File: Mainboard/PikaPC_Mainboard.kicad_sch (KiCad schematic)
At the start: 83 parts, among them J1 Conn_02x05_Odd_Even, J10 Conn_01x08, J11 Conn_01x08, J12 Conn_01x08, J13 Conn_01x08, J14 Conn_01x08, J15 Conn_01x08, J16 Conn_01x08, J17 Conn_01x08, J18 Conn_01x10, J19 Conn_02x05_Odd_Even, J5 DIN41612_03x32_C_Split, J6 Mini-DIN-6, J7 Mini-DIN-6, J8 Conn_01x06, J9 Conn_01x08, SW1 SW_Push_DPDT, SW2 SW_Push, U1 PPC403GA, U10 74LS07, U11 86C325, U12 GD75232N, U13 74LVC125, U14 MCP120-315GI/TO, U15 AS6C4008-55PCN, U16 AS6C4008-55PCN, U17 ATF1504, U18 T224162B, U19 T224162B, U2 SN74LVC245A, U20 T224162B, U21 T224162B, U3 SST39VF010, U4 SN74LVC245A, U5 SN74LVC245A, U6 SN74LVC245A, U7 8042 PS/2, U8 ATF22V10C, U9 74LS04, Y1 25M, Y2 7M3728, Y3 14M31818

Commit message: ViRGE schematic/layout cleanup
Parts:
- removed R12, R13, R14, R15, R16: 10k, Resistor_THT:R_Axial_DIN0204_L3.6mm_D1.6mm_P2.54mm_Vertical, symbol Device:R_Small_US
- removed R4: 147R, Resistor_THT:R_Axial_DIN0204_L3.6mm_D1.6mm_P2.54mm_Vertical, symbol Device:R_Small_US
- added R2: 220R, Resistor_THT:R_Axial_DIN0204_L3.6mm_D1.6mm_P2.54mm_Vertical, symbol Device:R_Small_US
- added R3: 470R, Resistor_THT:R_Axial_DIN0204_L3.6mm_D1.6mm_P2.54mm_Vertical, symbol Device:R_Small_US
- added RN5: 9A103J, Resistor_THT:R_Array_SIP9, symbol Device:R_Network08_US
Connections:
- net GND: now also R2.2, R3.2, RN5.1 (common)
- net INT0: now also RN5.7 (R6); no longer RN3.3 (R2)
- net INT1: now also U7.35 (KB-OBFO), RN5.8 (R7); no longer RN3.4 (R3)
- net INT2: now also U7.36 (MS-OBFO), RN5.9 (R8); no longer RN3.5 (R4)
- net PD1: now also RN5.2 (R1)
- net PD2: now also RN5.3 (R2)
- net PD4: now also RN5.4 (R3)
- net PD5: now also RN5.5 (R4)
- net PD6: now also RN5.6 (R5)
- net RSET: now also R2.1, R3.1
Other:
- note added: "RSET Target: 147R"
- moved on the sheet: C24, RN4, U10G, U11E, U9G

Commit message: ViRGE Strapping pulldowns should be on VMD not PD
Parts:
- added RN6: 9A103J, Resistor_THT:R_Array_SIP9, symbol Device:R_Network08_US
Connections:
- net GND: now also RN6.1 (common)
- net PD1: no longer RN5.2 (R1)
- net PD2: no longer RN5.3 (R2)
- net PD4: no longer RN5.4 (R3)
- net PD5: no longer RN5.5 (R4)
- net PD6: no longer RN5.6 (R5)
- net VMD1: now also RN6.2 (R1)
- net VMD2: now also RN6.3 (R2)
- net VMD4: now also RN6.4 (R3)
- net VMD5: now also RN6.5 (R4)
- net VMD6: now also RN6.6 (R5)
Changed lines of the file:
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@@
 	(wire
 		(pts
-			(xy 863.6 182.88) (xy 876.3 182.88)
+			(xy 1193.8 276.86) (xy 1206.5 276.86)
 		)
 		(stroke
@@
 	(wire
 		(pts
-			(xy 863.6 177.8) (xy 876.3 177.8)
+			(xy 1193.8 271.78) (xy 1206.5 271.78)
 		)
 		(stroke
@@
 	(wire
 		(pts
-			(xy 863.6 180.34) (xy 876.3 180.34)
+			(xy 1193.8 274.32) (xy 1206.5 274.32)
 		)
 		(stroke
@@
 	(wire
 		(pts
-			(xy 863.6 172.72) (xy 876.3 172.72)
+			(xy 1193.8 266.7) (xy 1206.5 266.7)
 		)
 		(stroke
@@
 	(wire
 		(pts
-			(xy 863.6 175.26) (xy 876.3 175.26)
+			(xy 1193.8 269.24) (xy 1206.5 269.24)
 		)
 		(stroke
@@
 		)
 	)
-	(label "PD1"
-		(at 863.6 172.72 0)
+	(label "VMD1"
+		(at 1193.8 266.7 0)
 		(effects
 			(font
@@
 		)
 	)
-	(label "PD2"
-		(at 863.6 175.26 0)
+	(label "VMD2"
+		(at 1193.8 269.24 0)
 		(effects
 			(font
@@
 		)
 	)
-	(label "PD6"
-		(at 863.6 182.88 0)
+	(label "VMD6"
+		(at 1193.8 276.86 0)
 		(effects
 			(font
@@
 		)
 	)
-	(label "PD5"
-		(at 863.6 180.34 0)
+	(label "VMD5"
+		(at 1193.8 274.32 0)
 		(effects
 			(font
@@
 		)
 	)
-	(label "PD4"
-		(at 863.6 177.8 0)
+	(label "VMD4"
+		(at 1193.8 271.78 0)
 		(effects
 			(font
@@
 	(symbol
 		(lib_id "power:GND")
+		(at 1216.66 266.7 90)
+		(unit 1)
+		(exclude_from_sim no)
+		(in_bom yes)
+		(on_board yes)
+		(dnp no)
+		(property "Reference" "#PWR069"
+			(at 1223.01 266.7 0)
+			(effects
+				(font
+					(size 1.27 1.27)
+				)
+				(hide yes)
+			)
+		)
+		(property "Value" "GND"
+			(at 1221.74 266.7 90)
+			(effects
+				(font
+					(size 1.27 1.27)
+				)
+			)
+		)
+		(property "Footprint" ""
+			(at 1216.66 266.7 0)
+			(effects
+				(font
+					(size 1.27 1.27)
+				)
+				(hide yes)
+			)
+		)
+		(property "Datasheet" ""
+			(at 1216.66 266.7 0)
+			(effects
+				(font
+					(size 1.27 1.27)
+				)
+				(hide yes)
+			)
+		)
+		(property "Description" "Power symbol creates a global label with name \"GND\" , ground"
+			(at 1216.66 266.7 0)
+			(effects
+				(font
+					(size 1.27 1.27)
+				)
+				(hide yes)
+			)
+		)
+		(pin "1"
+		)
+		(instances
+			(project "PikaPC_Mainboard"
+				(path "/31647a00-1631-4687-a4ca-8a073377aae5"
+					(reference "#PWR069")
+					(unit 1)
+				)
+			)
+		)
+	)
+	(symbol
+		(lib_id "power:GND")
 		(at 1087.12 200.66 270)
 		(unit 1)
@@
 				)
 			)
+		)
+	)
+	(symbol
+		(lib_id "Device:R_Network08_US")
+		(at 1211.58 276.86 270)
+		(unit 1)
+		(exclude_from_sim no)
+		(in_bom yes)
+		(on_board yes)
+		(dnp no)
+		(fields_autoplaced yes)
+		(property "Reference" "RN6"
+			(at 1211.326 261.2855 90)
+			(effects
+				(font
+					(size 1.27 1.27)
+				)
+			)
+		)
+		(property "Value" "9A103J"
+			(at 1211.326 263.7098 90)
+			(effects
+				(font
+					(size 1.27 1.27)
+				)
+			)
+		)
+		(property "Footprint" "Resistor_THT:R_Array_SIP9"
+			(at 1211.58 288.925 90)
+			(effects
+				(font
+					(size 1.27 1.27)
+				)
+				(hide yes)
+			)
+		)
+		(property "Datasheet" "http://www.vishay.com/docs/31509/csc.pdf"
+			(at 1211.58 276.86 0)
+			(effects
+				(font
+					(size 1.27 1.27)
+				)
+				(hide yes)
+			)
+		)
+		(property "Description" "8 resistor network, star topology, bussed resistors, small US symbol"
+			(at 1211.58 276.86 0)
+			(effects
+				(font
+					(size 1.27 1.27)
+				)
+				(hide yes)
+			)
+		)
+		(pin "5"
+		)
+		(pin "8"
+		)
+		(pin "7"
+		)
+		(pin "3"
+		)
+		(pin "1"
+		)
+		(pin "4"
+		)
+		(pin "6"
+		)
+		(pin "2"
+		)
+		(pin "9"
+		)
+		(instances
+			(project "PikaPC_Mainboard"
+				(path "/31647a00-1631-4687-a4ca-8a073377aae5"
+					(reference "RN6")
+					(unit 1)
+				)
+			)

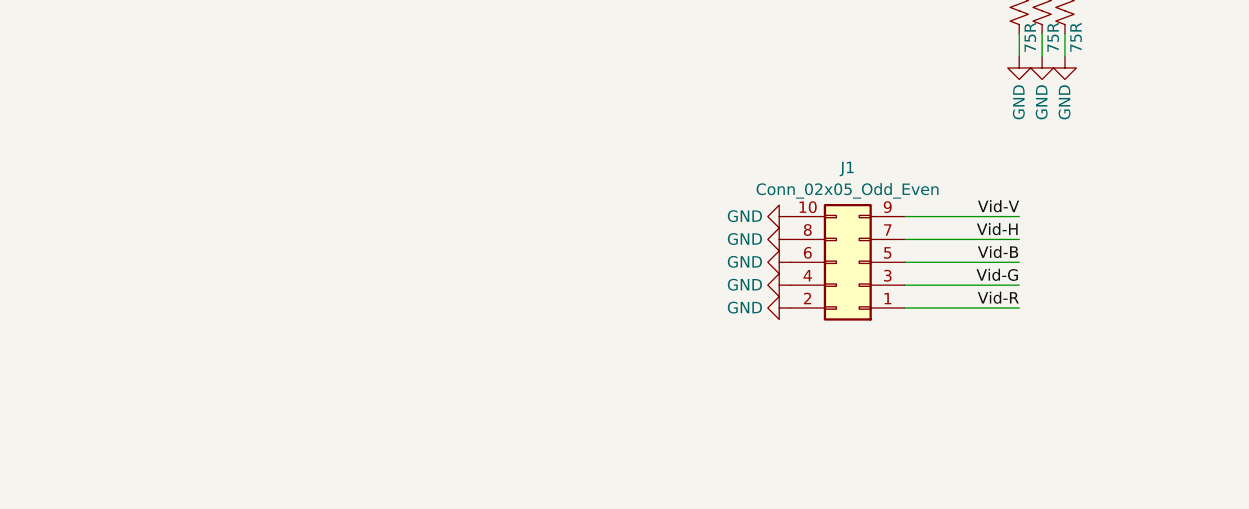
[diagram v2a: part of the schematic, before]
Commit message: VGA output use full-size header, add ferrite beads
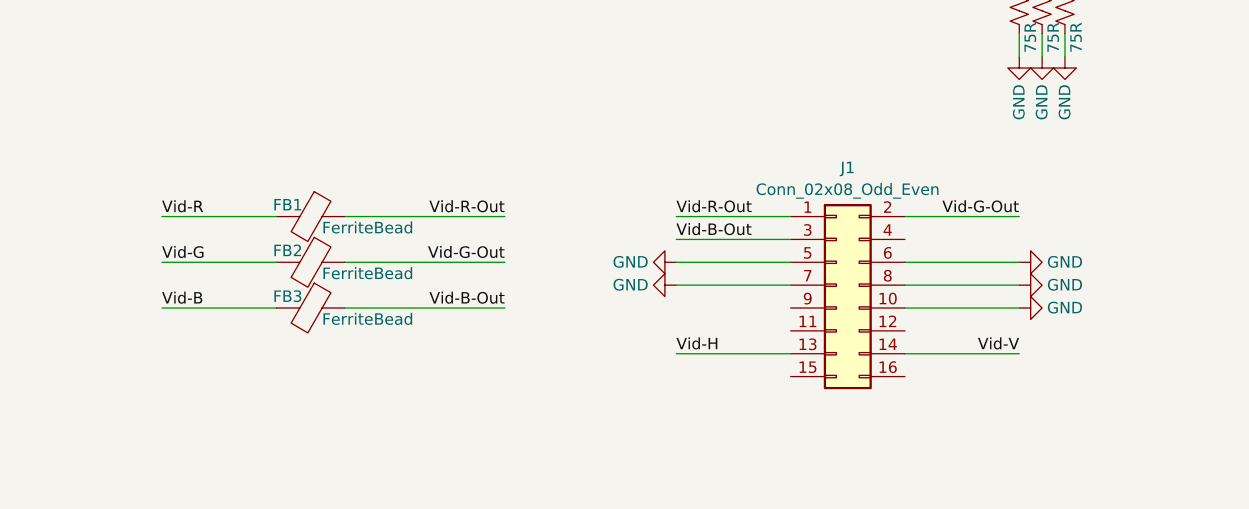
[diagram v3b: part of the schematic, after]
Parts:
- removed J1: Conn_02x05_Odd_Even, Connector_PinHeader_2.54mm:PinHeader_2x05_P2.54mm_Vertical, symbol Connector_Generic:Conn_02x05_Odd_Even
- added FB1, FB2, FB3: FerriteBead, Inductor_THT:L_Axial_L7.0mm_D3.3mm_P5.08mm_Vertical_Fastron_MICC, symbol Device:FerriteBead
- added J1: Conn_02x08_Odd_Even, Connector_PinHeader_2.54mm:PinHeader_2x08_P2.54mm_Vertical, symbol Connector_Generic:Conn_02x08_Odd_Even
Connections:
- net GND: now also J1.10 (Pin_10), J1.5 (Pin_5), J1.6 (Pin_6), J1.7 (Pin_7), J1.8 (Pin_8)
- net Vid-B: now also FB3.2
- net Vid-G: now also FB2.2
- net Vid-H: now also J1.13 (Pin_13)
- net Vid-R: now also FB1.2
- net Vid-V: now also J1.14 (Pin_14)
- new net Vid-B-Out: FB3.1, J1.3 (Pin_3)
- new net Vid-G-Out: FB2.1, J1.2 (Pin_2)
- new net Vid-R-Out: FB1.1, J1.1 (Pin_1)

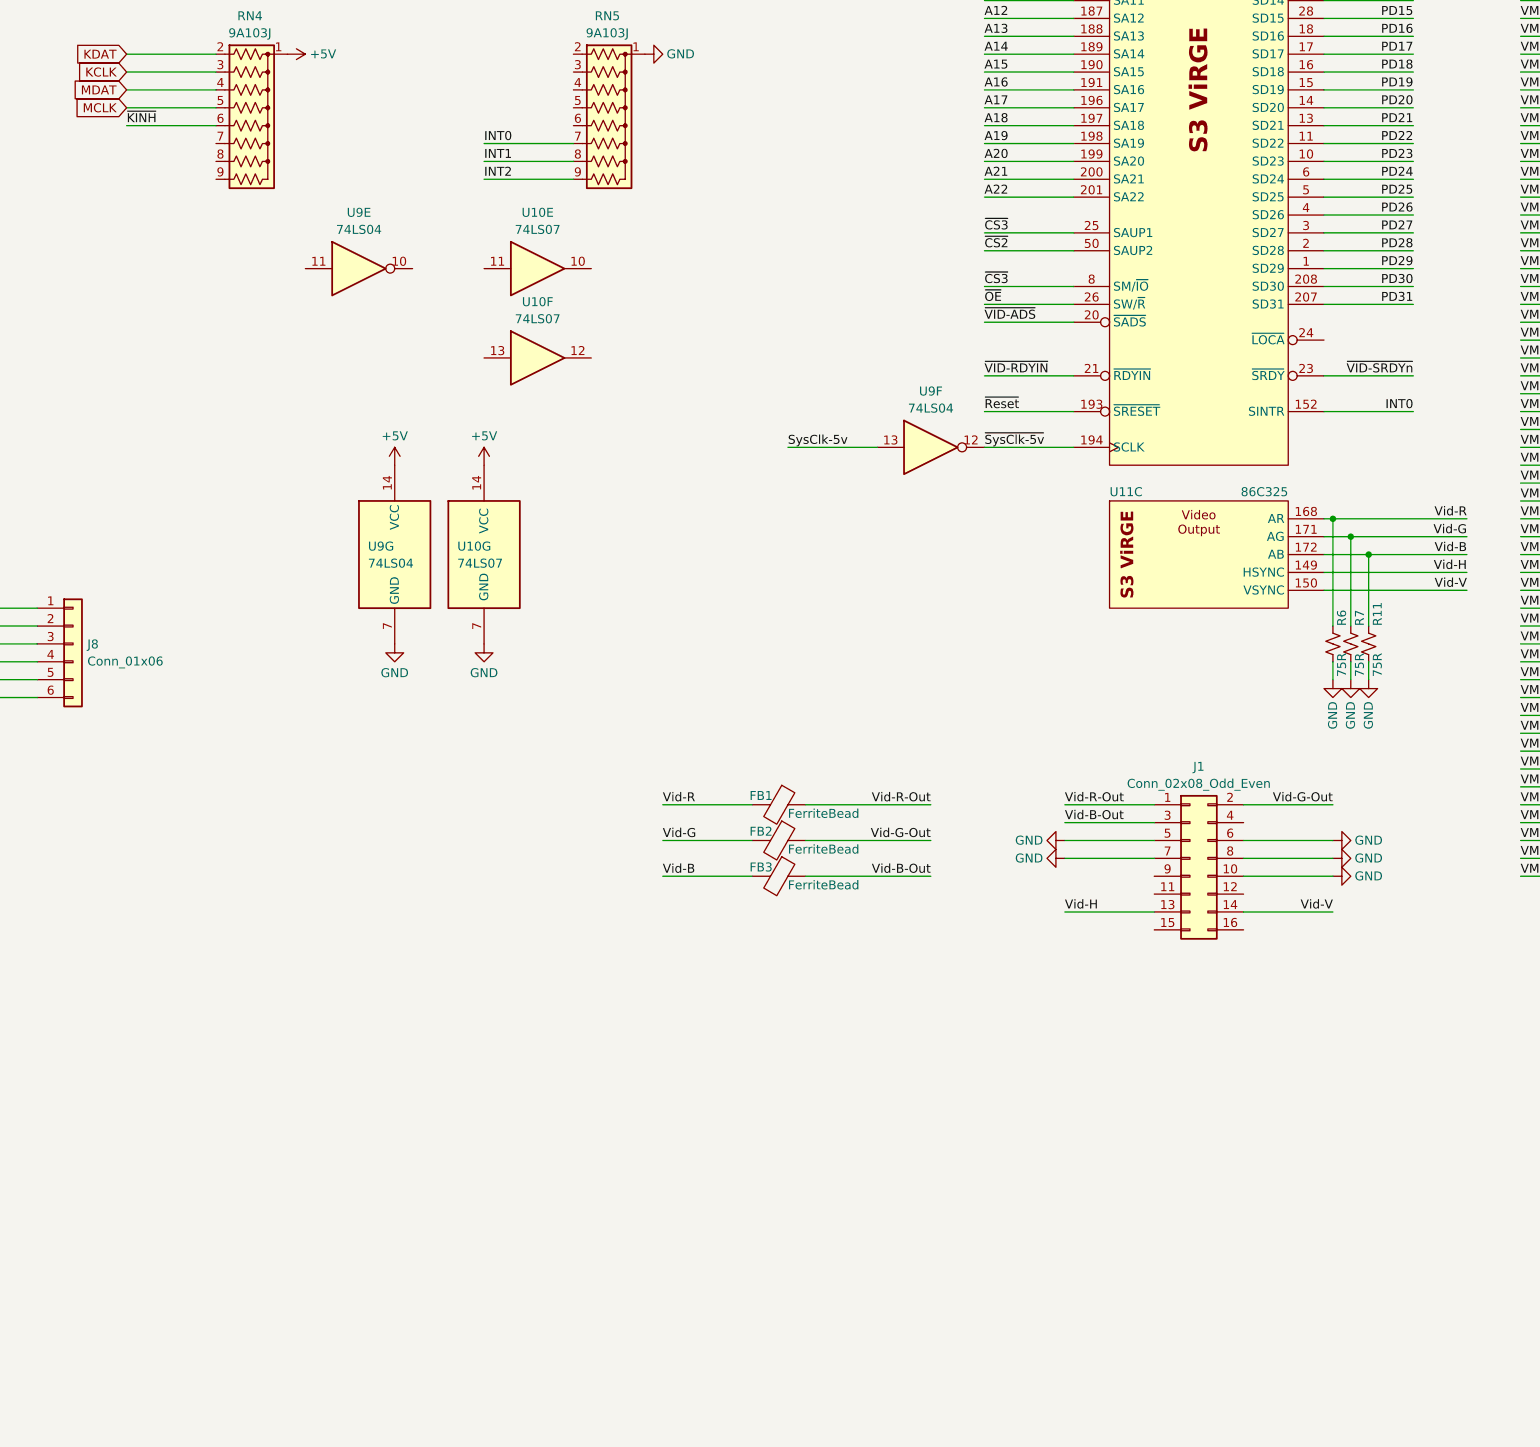
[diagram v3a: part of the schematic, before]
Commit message: Troubleshooting ViRGE communication
- use A[25:23] for ViRGE SAUP[2:1] & M/IO# signals
- add pull-up resistors to ViRGE ready & loca signals
- adjust bank registers for new memory map
- add forth test program for VGA init & ID
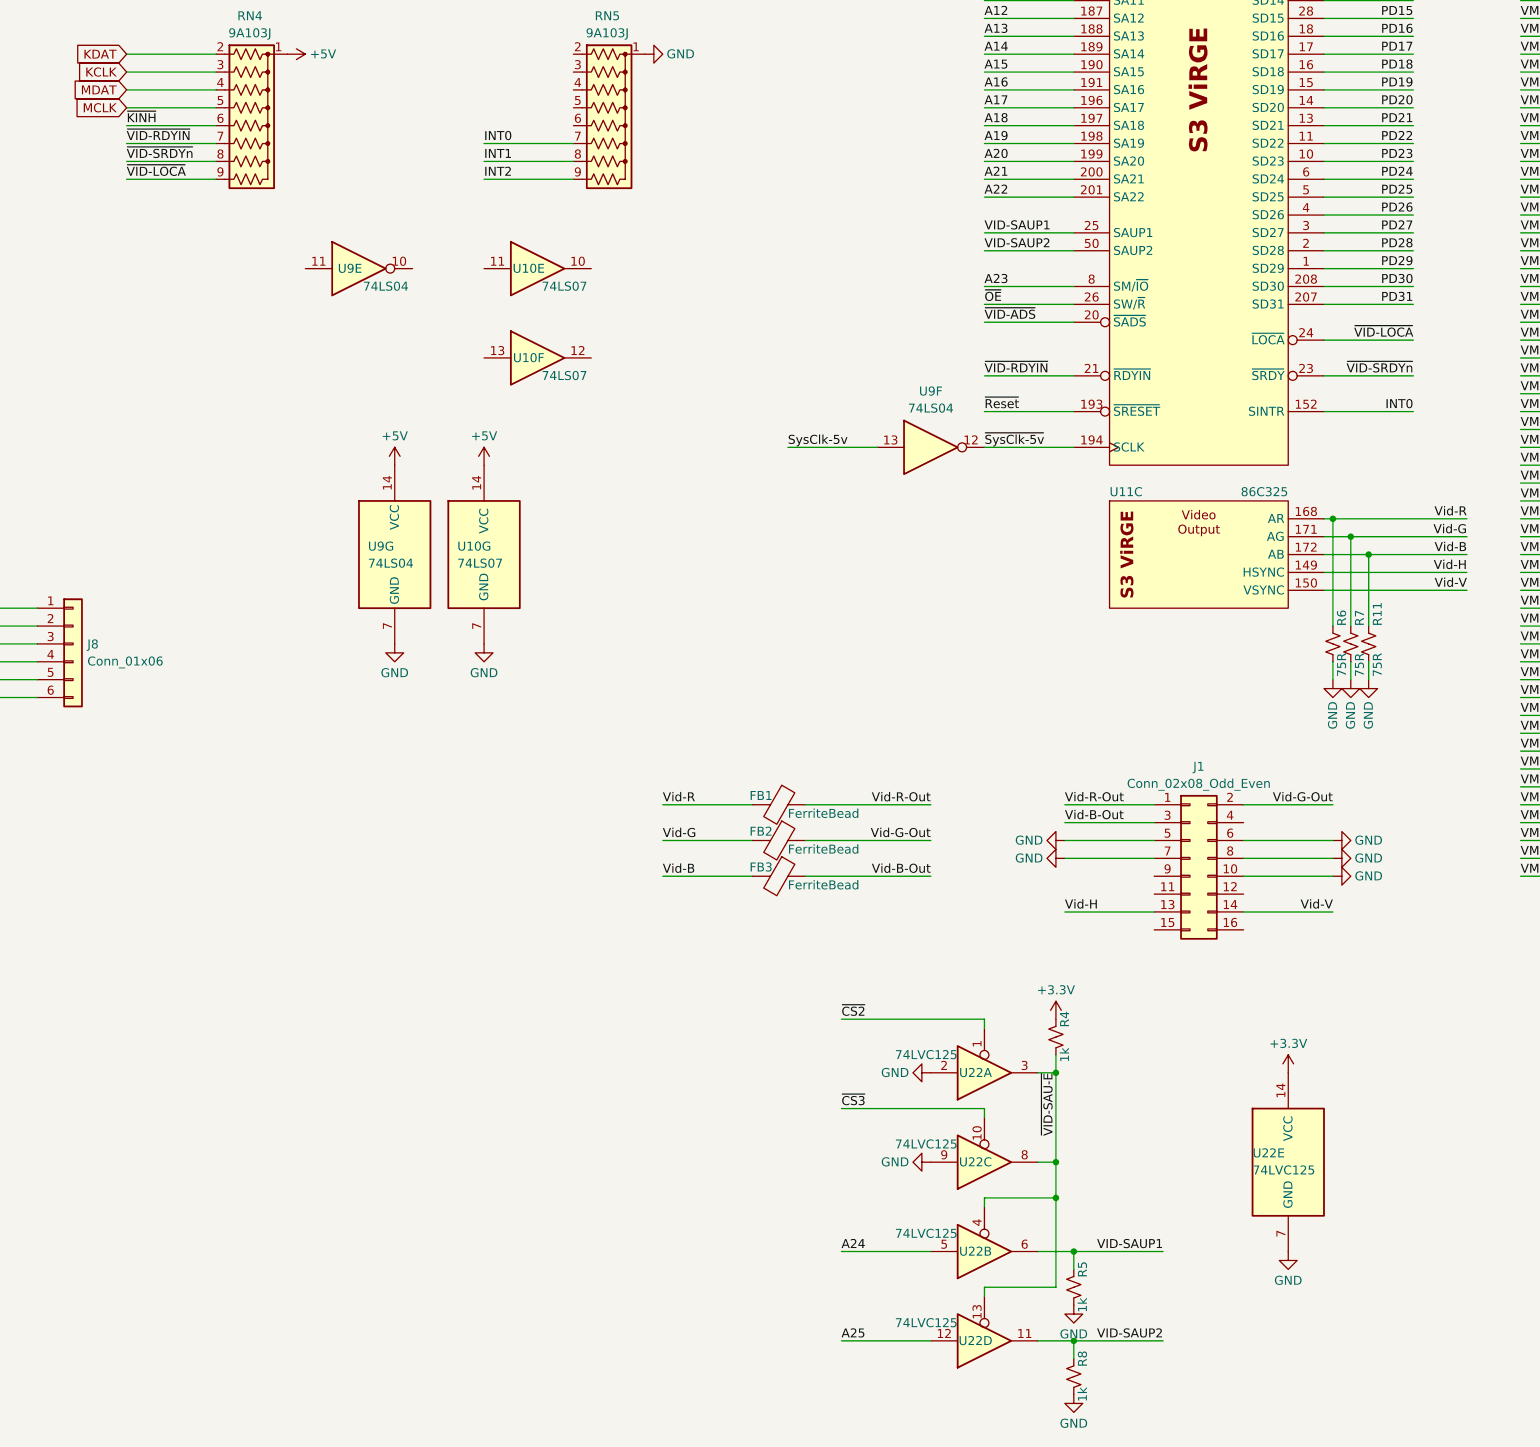
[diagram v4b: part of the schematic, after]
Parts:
- added R4, R5, R8: 1k, Resistor_THT:R_Axial_DIN0204_L3.6mm_D1.6mm_P7.62mm_Horizontal, symbol Device:R_Small_US
- added U22: 74LVC125, Package_DIP:DIP-14_W7.62mm_Socket, symbol 74xx:74LVC125
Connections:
- net +3.3V: now also R4.2, U22.14 (VCC)
- net A23: now also U11.8 (SM/~{IO})
- net A24: now also U22.5
- net A25: now also U22.12
- net GND: now also R5.1, R8.1, U22.2, U22.7 (GND), U22.9
- net ~{CS2}: now also U22.1; no longer U11.50 (SAUP2)
- net ~{CS3}: now also U22.10; no longer U11.25 (SAUP1), U11.8 (SM/~{IO})
- net ~{VID-RDYIN}: now also RN4.7 (R6)
- net ~{VID-SRDYn}: now also RN4.8 (R7)
- net ~{VID-LOCA}: now reaches U11.24 (~{LOCA})
- net ~{VID-LOCA}: now also RN4.9 (R8)
- new net VID-SAUP1: R5.2, U11.25 (SAUP1), U22.6
- new net VID-SAUP2: R8.2, U11.50 (SAUP2), U22.11
- new net ~{VID-SAU-E}: R4.1, U22.13, U22.3, U22.4, U22.8

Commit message: ViRGE byte select fixes
- swap data bus byte order
- decode low address bits for write byte selects
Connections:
- net PD0: now also U11.6 (SD24); no longer U11.46 (SD0)
- net PD1: now also U11.5 (SD25); no longer U11.45 (SD1)
- net PD10: now also U11.16 (SD18); no longer U11.34 (SD10)
- net PD11: now also U11.15 (SD19); no longer U11.33 (SD11)
- net PD12: now also U11.14 (SD20); no longer U11.31 (SD12)
- net PD13: now also U11.13 (SD21); no longer U11.30 (SD13)
- net PD14: now also U11.11 (SD22); no longer U11.29 (SD14)
- net PD15: now also U11.10 (SD23); no longer U11.28 (SD15)
- net PD16: now also U11.36 (SD8); no longer U11.18 (SD16)
- net PD17: now also U11.35 (SD9); no longer U11.17 (SD17)
- net PD18: now also U11.34 (SD10); no longer U11.16 (SD18)
- net PD19: now also U11.33 (SD11); no longer U11.15 (SD19)
- net PD2: now also U11.4 (SD26); no longer U11.44 (SD2)
- net PD20: now also U11.31 (SD12); no longer U11.14 (SD20)
- net PD21: now also U11.30 (SD13); no longer U11.13 (SD21)
- net PD22: now also U11.29 (SD14); no longer U11.11 (SD22)
- net PD23: now also U11.28 (SD15); no longer U11.10 (SD23)
- net PD24: now also U11.46 (SD0); no longer U11.6 (SD24)
- net PD25: now also U11.45 (SD1); no longer U11.5 (SD25)
- net PD26: now also U11.44 (SD2); no longer U11.4 (SD26)
- net PD27: now also U11.43 (SD3); no longer U11.3 (SD27)
- net PD28: now also U11.42 (SD4); no longer U11.2 (SD28)
- net PD29: now also U11.41 (SD5); no longer U11.1 (SD29)
- net PD3: now also U11.3 (SD27); no longer U11.43 (SD3)
- net PD30: now also U11.40 (SD6); no longer U11.208 (SD30)
- net PD31: now also U11.39 (SD7); no longer U11.207 (SD31)
- net PD4: now also U11.2 (SD28); no longer U11.42 (SD4)
- net PD5: now also U11.1 (SD29); no longer U11.41 (SD5)
- net PD6: now also U11.208 (SD30); no longer U11.40 (SD6)
- net PD7: now also U11.207 (SD31); no longer U11.39 (SD7)
- net PD8: now also U11.18 (SD16); no longer U11.36 (SD8)
- net PD9: now also U11.17 (SD17); no longer U11.35 (SD9)
- net A0/~{WBE3} renamed A0/~{WBE0}
- net A0/~{WBE0}: now also U8.7 (I7); no longer U8.10 (I10)
- net A1/~{WBE2} renamed A1/~{WBE1}
- net A1/~{WBE1}: now also U8.8 (I8); no longer U8.9 (I9)
- net ~{WBE0} renamed ~{WBE3}
- net ~{WBE3}: now also U8.10 (I10); no longer U8.7 (I7)
- net ~{WBE1} renamed ~{WBE2}
- net ~{WBE2}: now also U8.9 (I9); no longer U8.8 (I8)
